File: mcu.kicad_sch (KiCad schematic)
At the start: 36 parts, among them Q1 BC817, Q2 BC817, SW1 SW_Push, SW2 SW_Push, SW3 SW_Push, U4 ESP32-S3-WROOM-1, U5 CP2102N-A02-GQFN28R

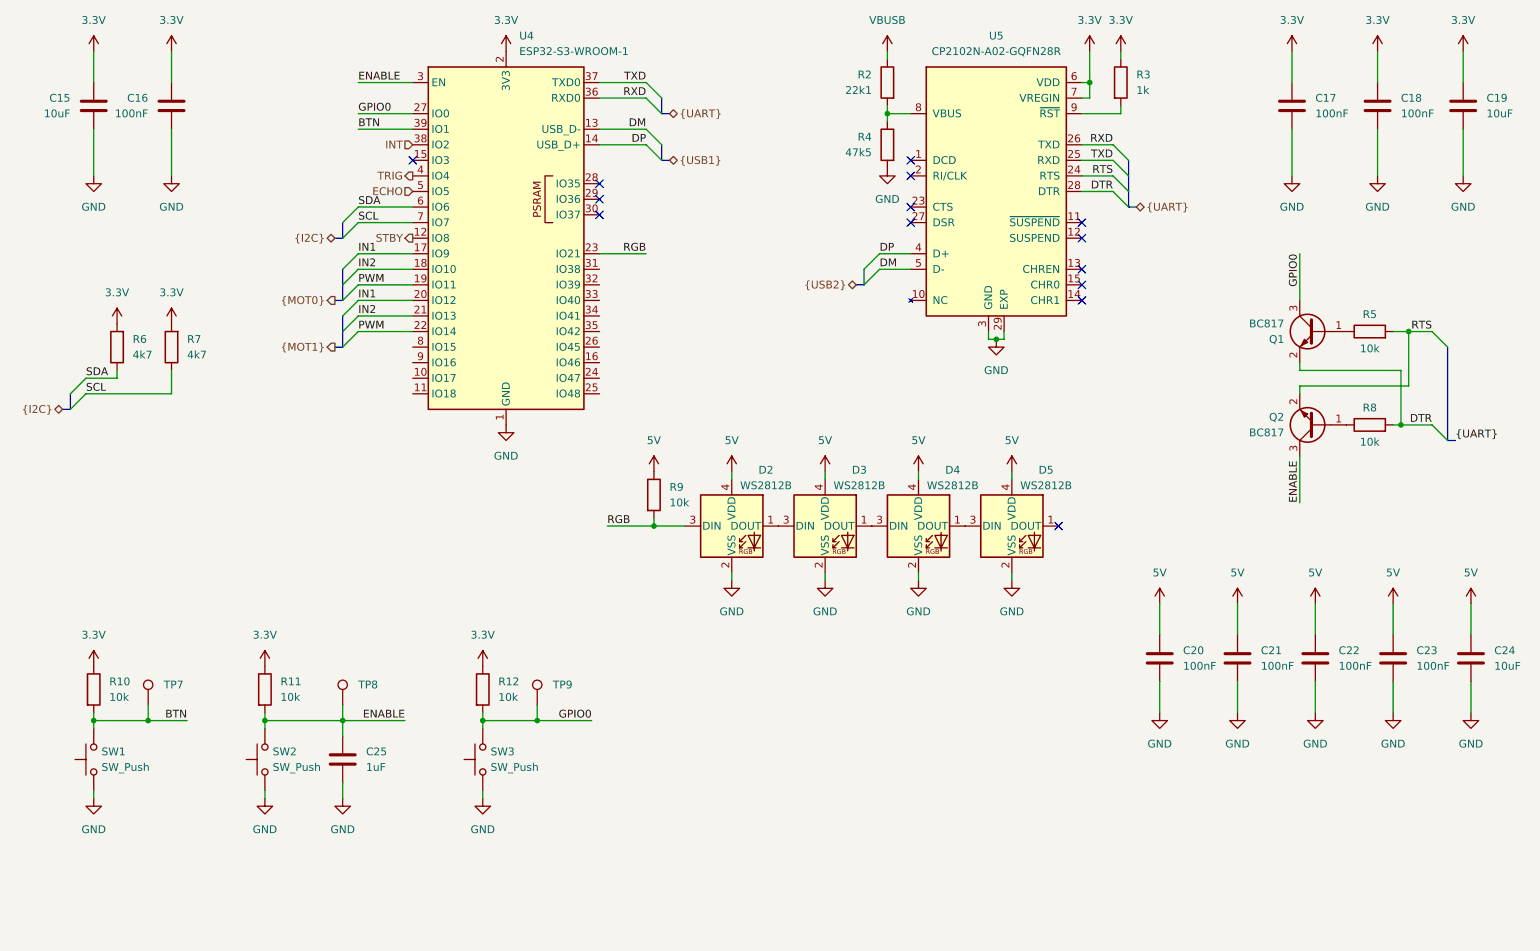
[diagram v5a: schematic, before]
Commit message: Add expansion pin headers
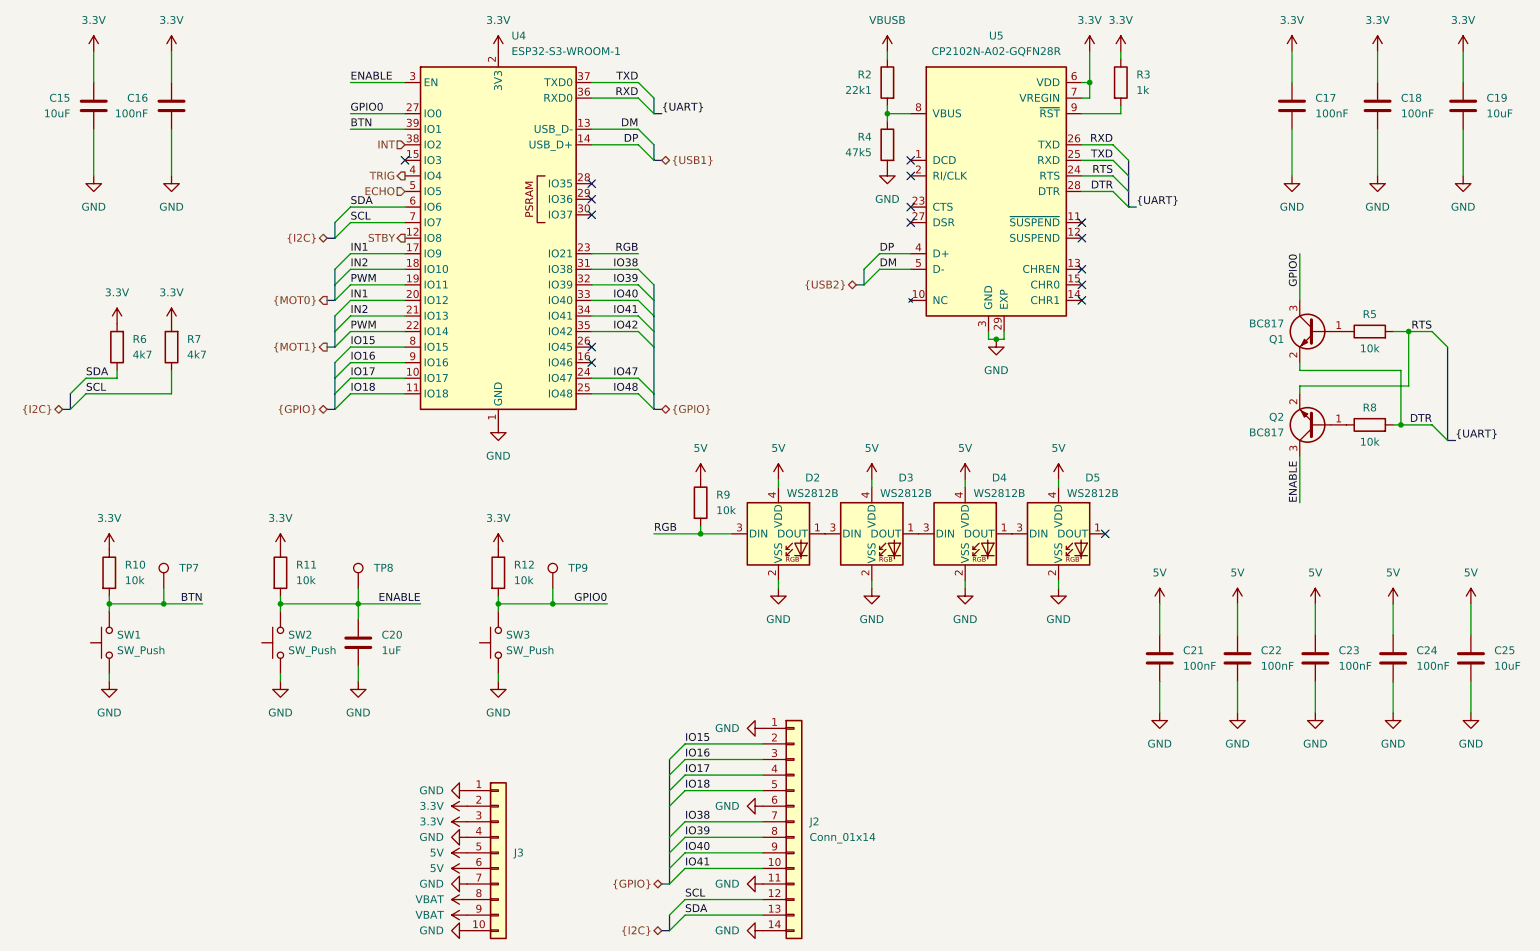
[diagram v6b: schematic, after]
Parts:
- added J2: Conn_01x14, symbol Connector_Generic:Conn_01x14
- added J3: Conn_01x10, Connector_PinHeader_2.54mm:PinHeader_1x10_P2.54mm_Vertical, symbol Connector_Generic:Conn_01x10
- renumbered C25 to C20, C20 to C21, C21 to C22, C22 to C23, C23 to C24, C24 to C25
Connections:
- net 3.3V: now also J3.2 (Pin_2), J3.3 (Pin_3)
- net 5V: now also J3.5 (Pin_5), J3.6 (Pin_6)
- net GND: now also J2.1 (Pin_1), J2.11 (Pin_11), J2.14 (Pin_14), J2.6 (Pin_6), J3.1 (Pin_1), J3.10 (Pin_10), J3.4 (Pin_4), J3.7 (Pin_7)
- net SCL: now also J2.12 (Pin_12)
- net SDA: now also J2.13 (Pin_13)
- net IO17: now reaches U4.10 (IO17)
- net IO17: now also J2.4 (Pin_4)
- net IO18: now reaches U4.11 (IO18)
- net IO18: now also J2.5 (Pin_5)
- net IO47: now reaches U4.24 (IO47)
- net IO48: now reaches U4.25 (IO48)
- net IO38: now reaches U4.31 (IO38)
- net IO38: now also J2.7 (Pin_7)
- net IO39: now reaches U4.32 (IO39)
- net IO39: now also J2.8 (Pin_8)
- net IO40: now reaches U4.33 (IO40)
- net IO40: now also J2.9 (Pin_9)
- net IO41: now reaches U4.34 (IO41)
- net IO41: now also J2.10 (Pin_10)
- net IO42: now reaches U4.35 (IO42)
- net IO15: now reaches U4.8 (IO15)
- net IO15: now also J2.2 (Pin_2)
- net IO16: now reaches U4.9 (IO16)
- net IO16: now also J2.3 (Pin_3)
- new net VBAT: J3.8 (Pin_8), J3.9 (Pin_9)
- no-connect marks 14 -> 16
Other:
- moved on the sheet: C20, D2, D3, D4, D5, R10, R11, R12, R9, SW1, SW2, SW3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

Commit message: Combine peripheral modules
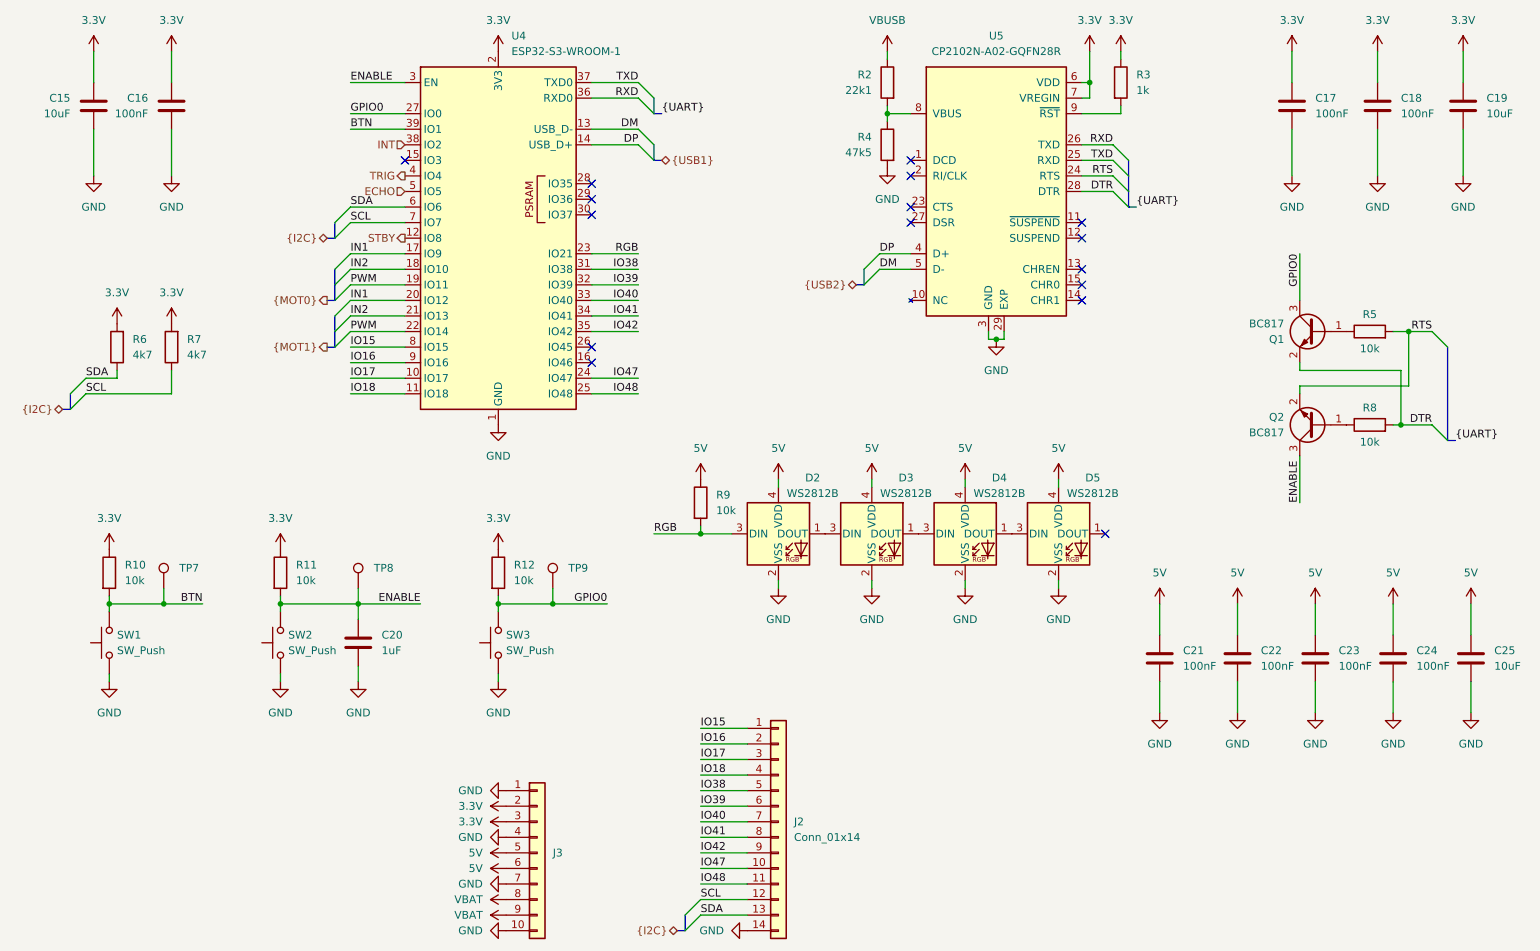
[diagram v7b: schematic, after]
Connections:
- net GND: no longer J2.1 (Pin_1), J2.11 (Pin_11), J2.6 (Pin_6)
- net IO15: now also J2.1 (Pin_1); no longer J2.2 (Pin_2)
- net IO16: now also J2.2 (Pin_2); no longer J2.3 (Pin_3)
- net IO17: now also J2.3 (Pin_3); no longer J2.4 (Pin_4)
- net IO18: now also J2.4 (Pin_4); no longer J2.5 (Pin_5)
- net IO38: now also J2.5 (Pin_5); no longer J2.7 (Pin_7)
- net IO39: now also J2.6 (Pin_6); no longer J2.8 (Pin_8)
- net IO40: now also J2.7 (Pin_7); no longer J2.9 (Pin_9)
- net IO41: now also J2.8 (Pin_8); no longer J2.10 (Pin_10)
- net IO42: now also J2.9 (Pin_9)
- net IO47: now also J2.10 (Pin_10)
- net IO48: now also J2.11 (Pin_11)
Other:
- moved on the sheet: J2, J3

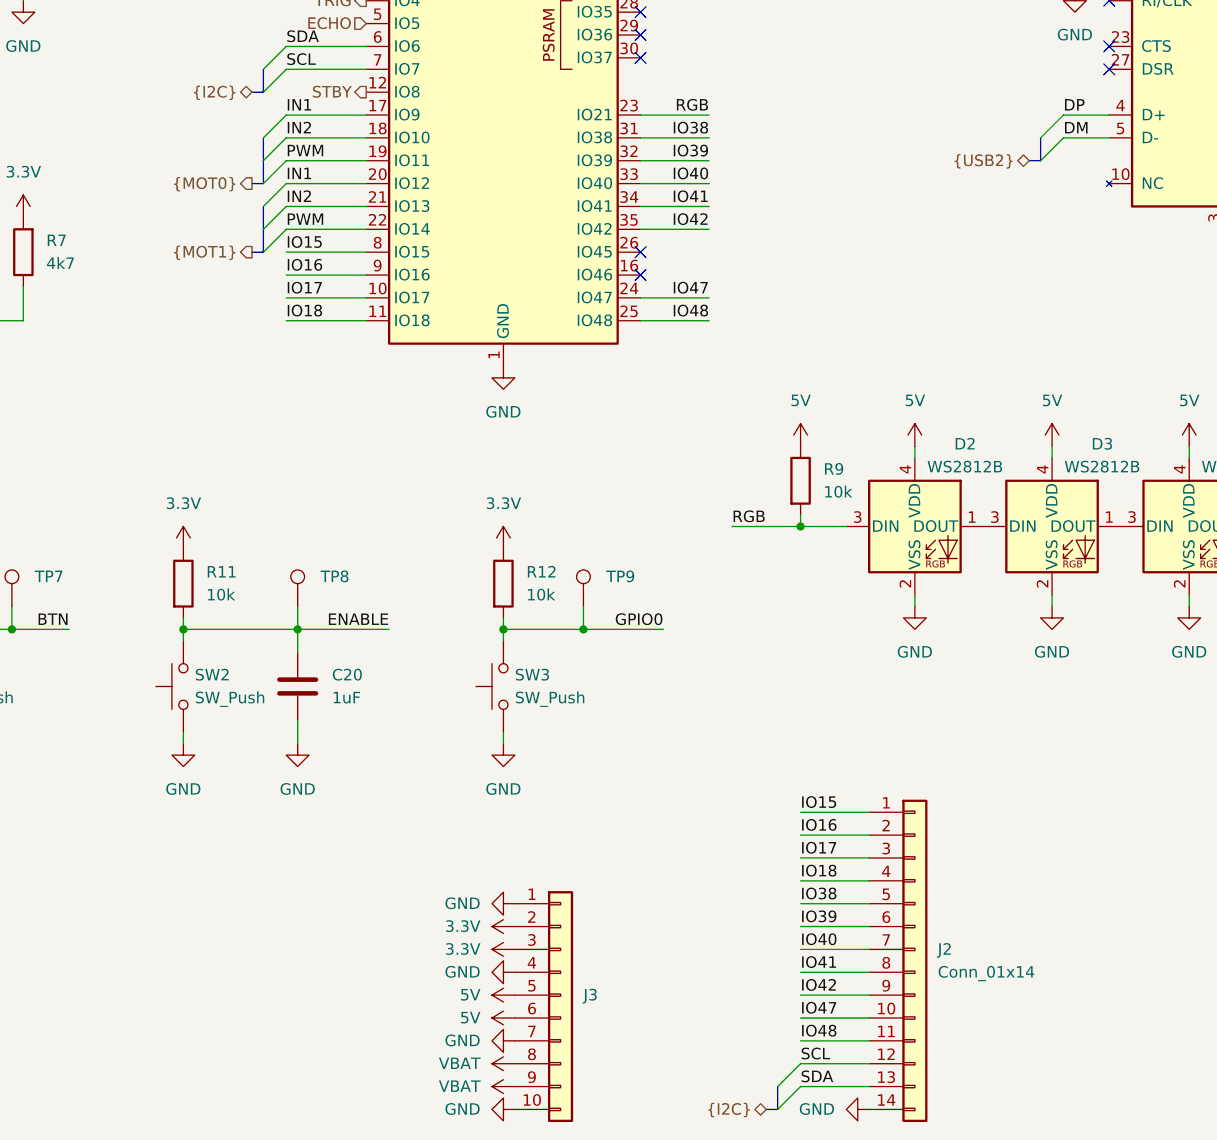
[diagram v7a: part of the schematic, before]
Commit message: Correct voltage level translation
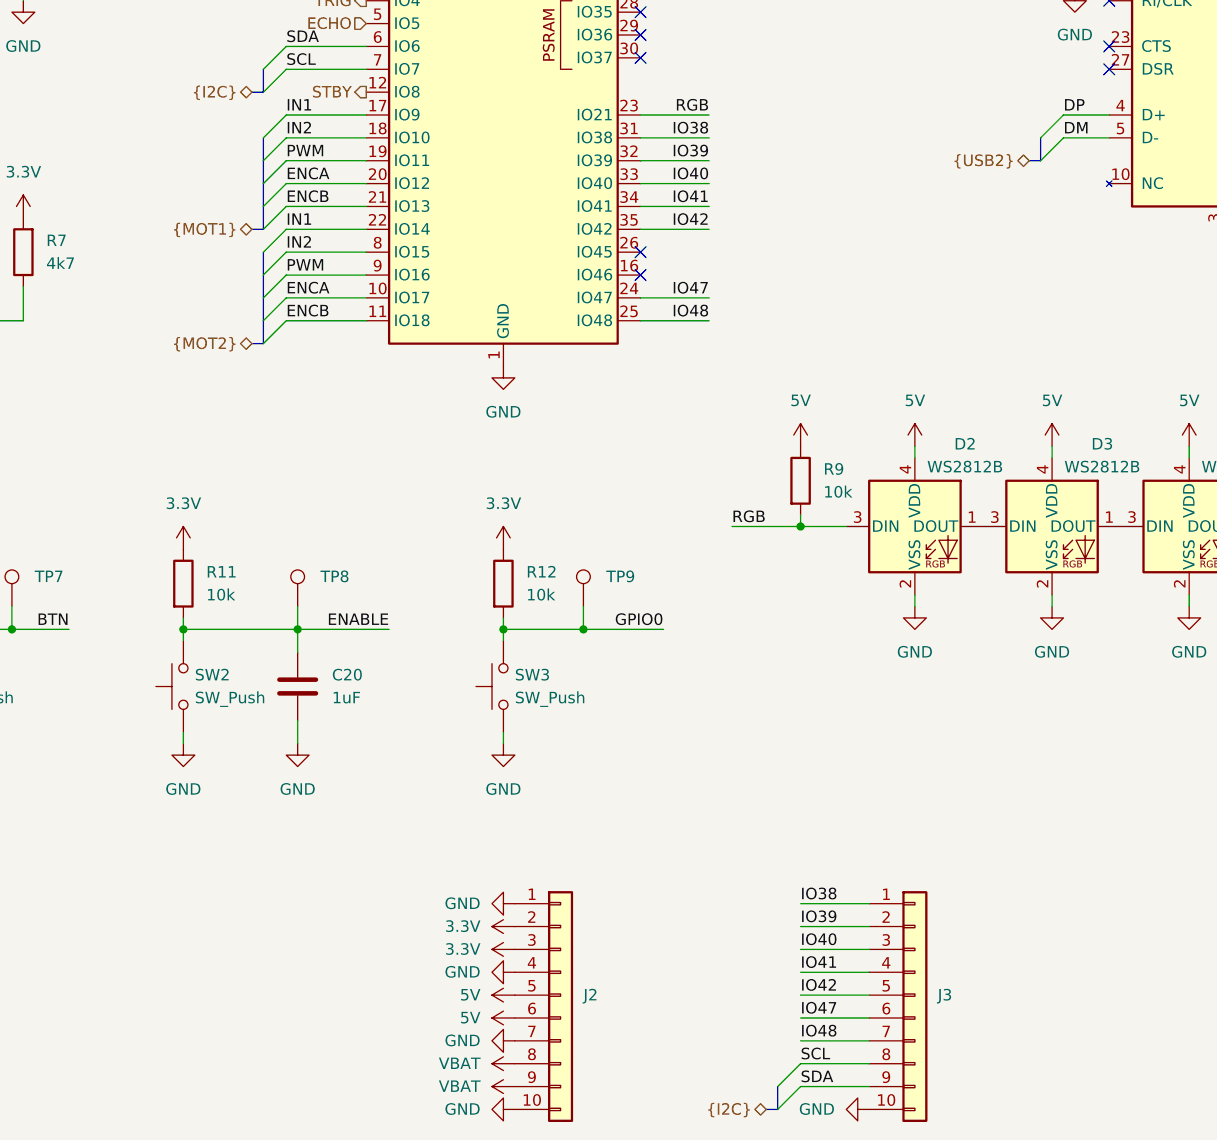
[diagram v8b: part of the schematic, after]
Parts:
- removed J2: Conn_01x14, symbol Connector_Generic:Conn_01x14
- added J3: Conn_01x10, Connector_PinHeader_2.54mm:PinHeader_1x10_P2.54mm_Vertical, symbol Connector_Generic:Conn_01x10
- renumbered J3 to J2
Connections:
- net IO15 is gone; now on net IN2: U4.8 (IO15)
- net IO16 is gone; now on net PWM: U4.9 (IO16)
- net GND: now also J3.10 (Pin_10)
- net IN1: now also U4.22 (IO14); no longer U4.20 (IO12)
- net IN2: no longer U4.21 (IO13)
- net IO38: now also J3.1 (Pin_1)
- net IO39: now also J3.2 (Pin_2)
- net IO40: now also J3.3 (Pin_3)
- net IO41: now also J3.4 (Pin_4)
- net IO42: now also J3.5 (Pin_5)
- net IO47: now also J3.6 (Pin_6)
- net IO48: now also J3.7 (Pin_7)
- net PWM: no longer U4.22 (IO14)
- net SCL: now also J3.8 (Pin_8)
- net SDA: now also J3.9 (Pin_9)
- net IO17 renamed ENCA
- net ENCA: now also U4.20 (IO12)
- net IO18 renamed ENCB
- net ENCB: now also U4.21 (IO13)
